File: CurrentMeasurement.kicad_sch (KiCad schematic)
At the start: 3 parts

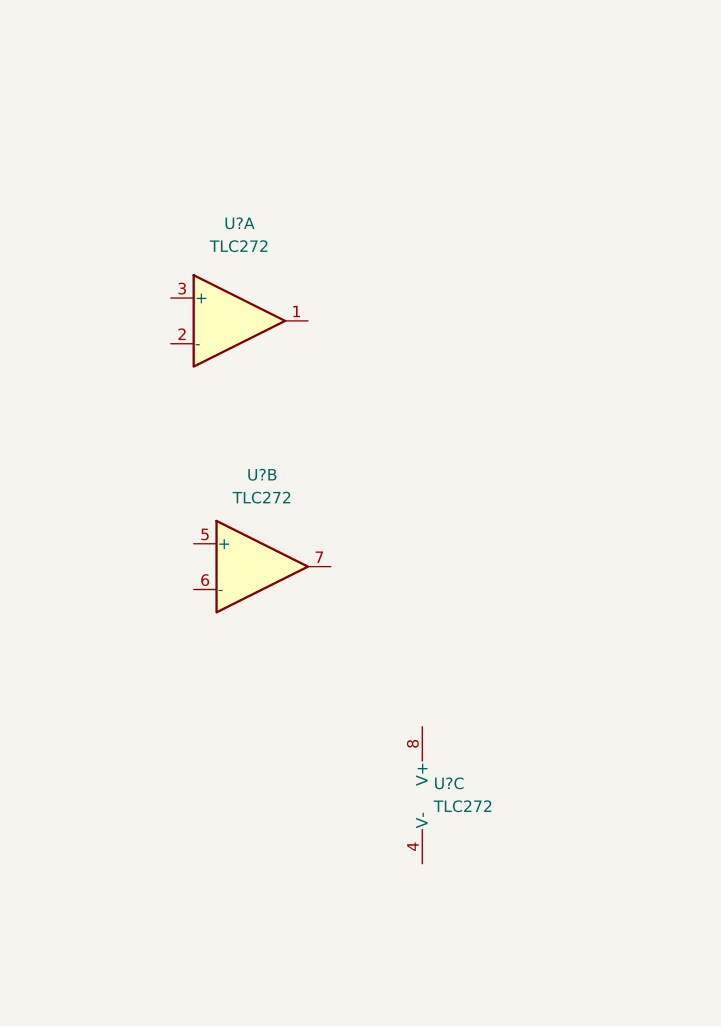
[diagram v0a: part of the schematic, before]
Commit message: added TIA schematic
started with TLC272
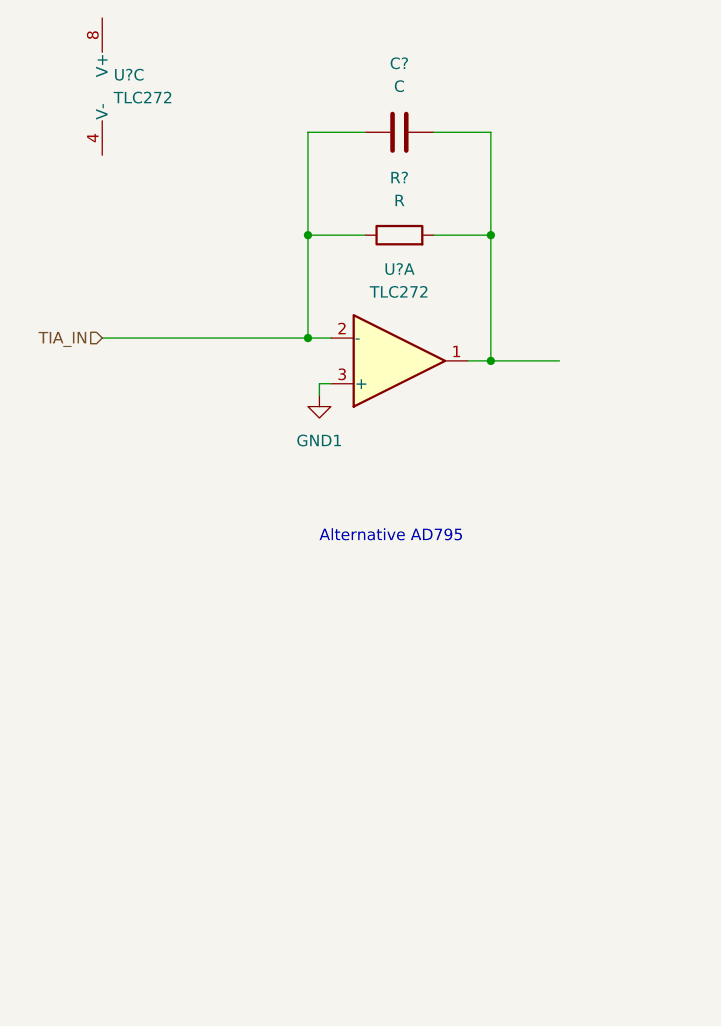
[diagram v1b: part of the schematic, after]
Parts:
- removed U?: TLC272, symbol Amplifier_Operational:TLC272
- added C?: C, symbol Device:C
- added R?: R, symbol Device:R
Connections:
- net at U?.1: now also C?.2, R?.2
- net TIA_IN: now reaches U?.2 (-)
- net TIA_IN: now also C?.1, R?.1
- net GND1: now reaches U?.3 (+)
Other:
- note added: "Alternative AD795"
- moved on the sheet: U?A, U?C
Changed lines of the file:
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@@
 (kicad_sch (version 20211123) (generator eeschema)
   (paper "A4")
+  (junction (at 93.98 52.07) (diameter 0) (color 0 0 0 0)
+  )
+  (junction (at 93.98 66.04) (diameter 0) (color 0 0 0 0)
+  )
+  (junction (at 73.66 52.07) (diameter 0) (color 0 0 0 0)
+  )
+  (junction (at 73.66 63.5) (diameter 0) (color 0 0 0 0)
+  )
+  (wire (pts (xy 73.66 40.64) (xy 73.66 52.07))
+    (stroke (width 0) (type default) (color 0 0 0 0))
+  )
+  (wire (pts (xy 91.44 66.04) (xy 93.98 66.04))
+    (stroke (width 0) (type default) (color 0 0 0 0))
+  )
+  (wire (pts (xy 87.63 40.64) (xy 93.98 40.64))
+    (stroke (width 0) (type default) (color 0 0 0 0))
+  )
+  (wire (pts (xy 80.01 40.64) (xy 73.66 40.64))
+    (stroke (width 0) (type default) (color 0 0 0 0))
+  )
+  (wire (pts (xy 73.66 52.07) (xy 73.66 63.5))
+    (stroke (width 0) (type default) (color 0 0 0 0))
+  )
+  (wire (pts (xy 87.63 52.07) (xy 93.98 52.07))
+    (stroke (width 0) (type default) (color 0 0 0 0))
+  )
+  (wire (pts (xy 93.98 52.07) (xy 93.98 66.04))
+    (stroke (width 0) (type default) (color 0 0 0 0))
+  )
+  (wire (pts (xy 76.2 68.58) (xy 74.93 68.58))
+    (stroke (width 0) (type default) (color 0 0 0 0))
+  )
+  (wire (pts (xy 74.93 68.58) (xy 74.93 69.85))
+    (stroke (width 0) (type default) (color 0 0 0 0))
+  )
+  (wire (pts (xy 93.98 66.04) (xy 101.6 66.04))
+    (stroke (width 0) (type default) (color 0 0 0 0))
+  )
+  (wire (pts (xy 50.8 63.5) (xy 73.66 63.5))
+    (stroke (width 0) (type default) (color 0 0 0 0))
+  )
+  (wire (pts (xy 80.01 52.07) (xy 73.66 52.07))
+    (stroke (width 0) (type default) (color 0 0 0 0))
+  )
+  (wire (pts (xy 93.98 40.64) (xy 93.98 52.07))
+    (stroke (width 0) (type default) (color 0 0 0 0))
+  )
+  (wire (pts (xy 73.66 63.5) (xy 76.2 63.5))
+    (stroke (width 0) (type default) (color 0 0 0 0))
+  )
+  (text "Alternative AD795" (at 74.93 86.36 0)
+    (effects (font (size 1.27 1.27)) (justify left bottom))
+  )
   (text "(High Precision)\nultra low current measurement" (at 179.07 178.435 0)
     (effects (font (size 3 3)) (justify left bottom))
   )
-  (symbol (lib_id "Amplifier_Operational:TLC272") (at 66.04 61.595 0) (unit 1)
+  (hierarchical_label "TIA_IN" (shape input) (at 50.8 63.5 180)
+    (effects (font (size 1.27 1.27)) (justify right))
+  )
+  (symbol (lib_id "Device:C") (at 83.82 40.64 90) (unit 1)
     (in_bom yes) (on_board yes) (fields_autoplaced)
-    (property "Reference" "U?" (id 0) (at 66.04 50.8 0))
-    (property "Value" "TLC272" (id 1) (at 66.04 53.34 0))
-    (property "Footprint" "" (id 2) (at 66.04 61.595 0)
+    (property "Reference" "C?" (id 0) (at 83.82 33.02 90))
+    (property "Value" "C" (id 1) (at 83.82 35.56 90))
+    (property "Footprint" "" (id 2) (at 87.63 39.6748 0)
       (effects (font (size 1.27 1.27)) hide)
     )
-    (property "Datasheet" "http://www.ti.com/lit/ds/symlink/tlc272.pdf" (id 3) (at 66.04 61.595 0)
+    (property "Datasheet" "~" (id 3) (at 83.82 40.64 0)
+      (effects (font (size 1.27 1.27)) hide)
+    )
+    (pin "1")
+    (pin "2")
+  )
+  (symbol (lib_id "power:GND1") (at 74.93 69.85 0) (unit 1)
+    (in_bom yes) (on_board yes) (fields_autoplaced)
+    (property "Reference" "#PWR?" (id 0) (at 74.93 76.2 0)
+      (effects (font (size 1.27 1.27)) hide)
+    )
+    (property "Value" "GND1" (id 1) (at 74.93 74.93 0))
+    (property "Footprint" "" (id 2) (at 74.93 69.85 0)
+      (effects (font (size 1.27 1.27)) hide)
+    )
+    (property "Datasheet" "" (id 3) (at 74.93 69.85 0)
+      (effects (font (size 1.27 1.27)) hide)
+    )
+    (pin "1")
+  )
+  (symbol (lib_id "Amplifier_Operational:TLC272") (at 83.82 66.04 0) (mirror x) (unit 1)
+    (in_bom yes) (on_board yes) (fields_autoplaced)
+    (property "Reference" "U?" (id 0) (at 83.82 55.88 0))
+    (property "Value" "TLC272" (id 1) (at 83.82 58.42 0))
+    (property "Footprint" "" (id 2) (at 83.82 66.04 0)
+      (effects (font (size 1.27 1.27)) hide)
+    )
+    (property "Datasheet" "http://www.ti.com/lit/ds/symlink/tlc272.pdf" (id 3) (at 83.82 66.04 0)
       (effects (font (size 1.27 1.27)) hide)
     )
@@
     (pin "8")
   )
-  (symbol (lib_id "Amplifier_Operational:TLC272") (at 88.9 114.3 0) (unit 3)
+  (symbol (lib_id "Device:R") (at 83.82 52.07 90) (unit 1)
     (in_bom yes) (on_board yes) (fields_autoplaced)
-    (property "Reference" "U?" (id 0) (at 87.63 113.0299 0)
-      (effects (font (size 1.27 1.27)) (justify left))
-    )
-    (property "Value" "TLC272" (id 1) (at 87.63 115.5699 0)
-      (effects (font (size 1.27 1.27)) (justify left))
-    )
-    (property "Footprint" "" (id 2) (at 88.9 114.3 0)
+    (property "Reference" "R?" (id 0) (at 83.82 45.72 90))
+    (property "Value" "R" (id 1) (at 83.82 48.26 90))
+    (property "Footprint" "" (id 2) (at 83.82 53.848 90)
       (effects (font (size 1.27 1.27)) hide)
     )
-    (property "Datasheet" "http://www.ti.com/lit/ds/symlink/tlc272.pdf" (id 3) (at 88.9 114.3 0)
+    (property "Datasheet" "~" (id 3) (at 83.82 52.07 0)
       (effects (font (size 1.27 1.27)) hide)
     )
     (pin "1")
     (pin "2")
-    (pin "3")
-    (pin "5")
-    (pin "6")
-    (pin "7")
-    (pin "4")
-    (pin "8")
   )
-  (symbol (lib_id "Amplifier_Operational:TLC272") (at 68.58 88.9 0) (unit 2)
+  (symbol (lib_id "Amplifier_Operational:TLC272") (at 53.34 35.56 0) (unit 3)
     (in_bom yes) (on_board yes) (fields_autoplaced)
-    (property "Reference" "U?" (id 0) (at 68.58 78.74 0))
-    (property "Value" "TLC272" (id 1) (at 68.58 81.28 0))
-    (property "Footprint" "" (id 2) (at 68.58 88.9 0)
+    (property "Reference" "U?" (id 0) (at 52.07 34.2899 0)
+      (effects (font (size 1.27 1.27)) (justify left))
+    )
+    (property "Value" "TLC272" (id 1) (at 52.07 36.8299 0)
+      (effects (font (size 1.27 1.27)) (justify left))
+    )
+    (property "Footprint" "" (id 2) (at 53.34 35.56 0)
       (effects (font (size 1.27 1.27)) hide)
     )
-    (property "Datasheet" "http://www.ti.com/lit/ds/symlink/tlc272.pdf" (id 3) (at 68.58 88.9 0)
+    (property "Datasheet" "http://www.ti.com/lit/ds/symlink/tlc272.pdf" (id 3) (at 53.34 35.56 0)
       (effects (font (size 1.27 1.27)) hide)
     )

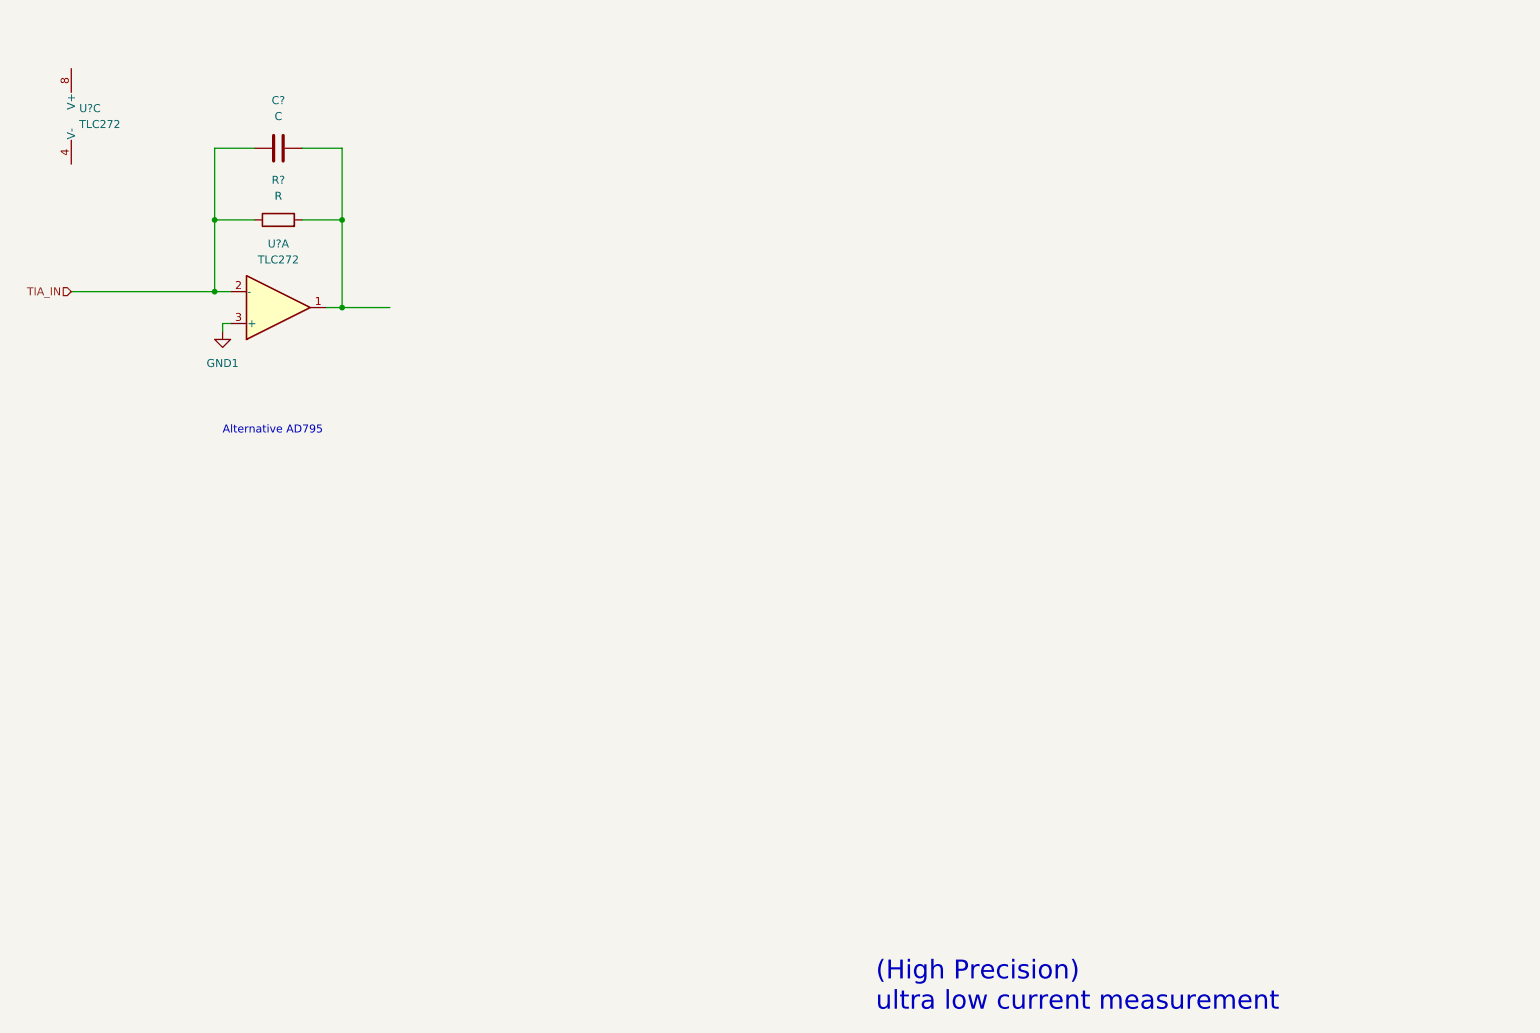
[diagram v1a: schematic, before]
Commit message: changed from TIA to DDC112, because this might be the simpler approach
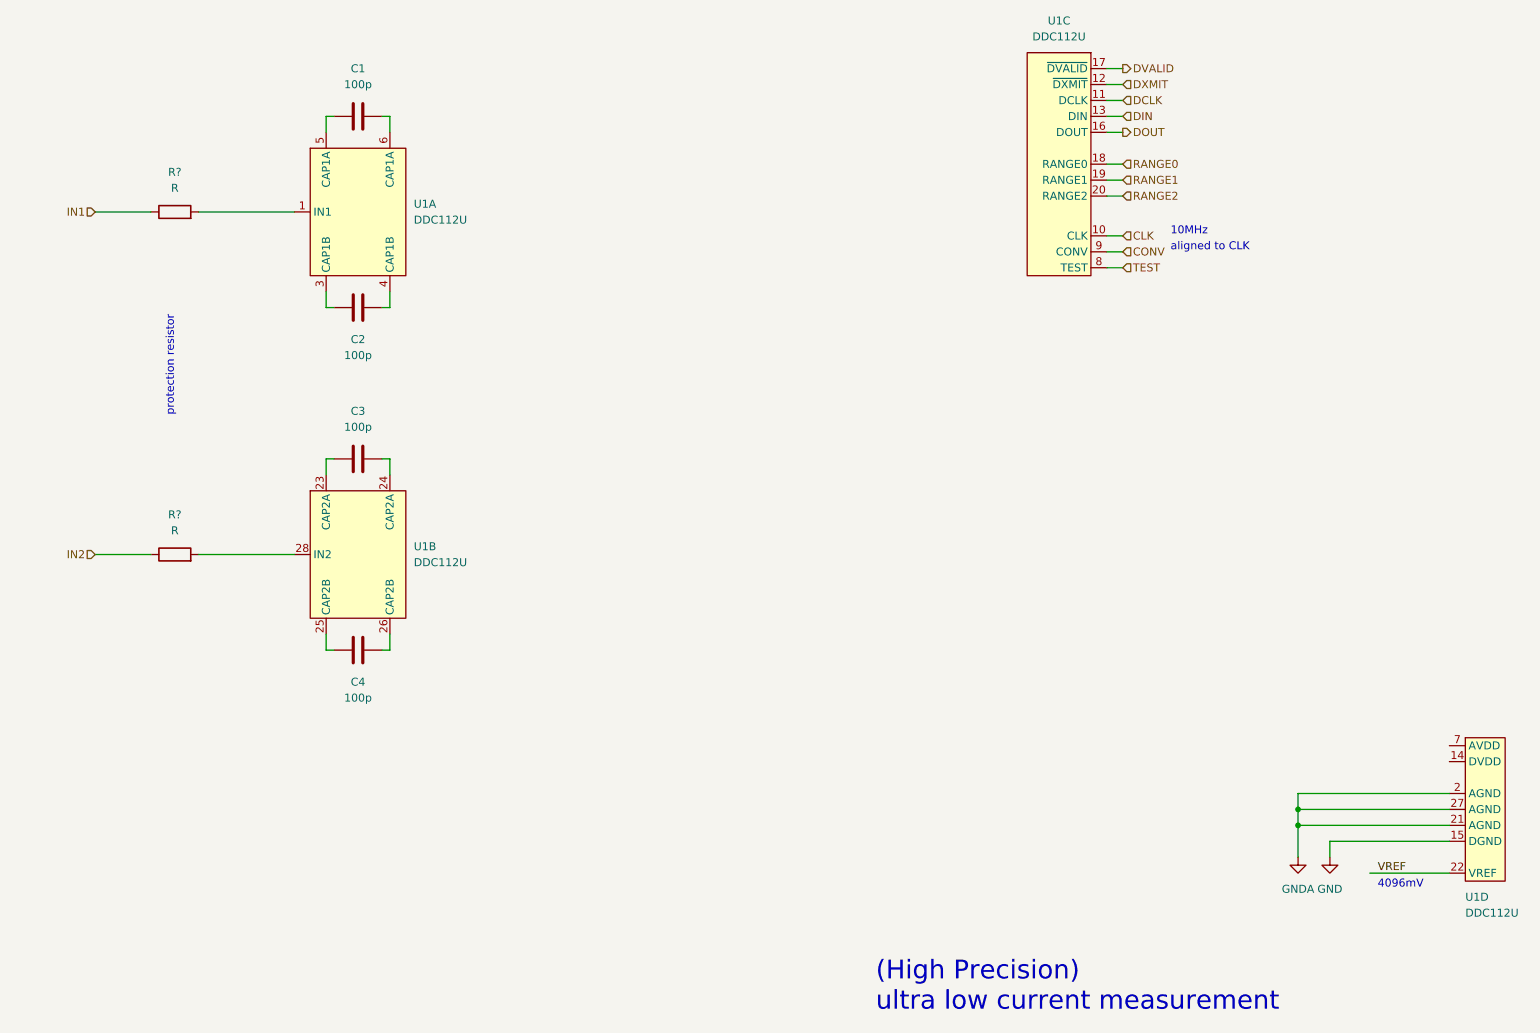
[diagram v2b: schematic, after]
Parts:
- removed C?: C, symbol Device:C
- removed R?: R, symbol Device:R
- removed U? (x2): TLC272, symbol Amplifier_Operational:TLC272
- added C1, C2, C3, C4: 100p, Capacitor_SMD:C_0402_1005Metric_Pad0.74x0.62mm_HandSolder, symbol Device:C
- added R? (x2): R, symbol Device:R
- added U1: DDC112U, Package_SO:SOIC-28W_7.5x17.9mm_P1.27mm, symbol DDC112:DDC112U
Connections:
- new net: C3.1, U1.23 (CAP2A)
- new net: C3.2, U1.24 (CAP2A)
- new net: C2.1, U1.3 (CAP1B)
- new net: C2.2, U1.4 (CAP1B)
- new net: C4.1, U1.25 (CAP2B)
- new net: C4.2, U1.26 (CAP2B)
- new net: R?.2, U1.28 (IN2)
- new net: R?.2, U1.1 (IN1)
- new net: C1.1, U1.5 (CAP1A)
- new net: C1.2, U1.6 (CAP1A)
- new net CLK: U1.10 (CLK)
- new net CONV: U1.9 (CONV)
- new net DCLK: U1.11 (DCLK)
- new net DIN: U1.13 (DIN)
- new net DOUT: U1.16 (DOUT)
- new net DVALID: U1.17 (~{DVALID})
- new net DXMIT: U1.12 (~{DXMIT})
- new net GND: U1.15 (DGND)
- new net GNDA: U1.2 (AGND), U1.21 (AGND), U1.27 (AGND)
- new net IN1: R?.1
- new net IN2: R?.1
- new net RANGE0: U1.18 (RANGE0)
- new net RANGE1: U1.19 (RANGE1)
- new net RANGE2: U1.20 (RANGE2)
- new net TEST: U1.8 (TEST)
- new net VREF: U1.22 (VREF)
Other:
- note added: "10MHz"
- note added: "4096mV"
- note added: "aligned to CLK"
- note added: "protection resistor"
- note removed: "Alternative AD795"
